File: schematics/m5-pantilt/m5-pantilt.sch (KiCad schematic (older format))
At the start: 23 parts, among them J1 Conn_02x15_Odd_Even, J2 Conn_02x03_Odd_Even, J3 Conn_02x03_Odd_Even, J4 Conn_01x04, J5 BAT, J6 Conn_01x04, J7 5V_POWER, SW1 SW_SPDT, U1 NL27WZ125

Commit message: Update to v0.2.0
Support another Three-State Bus Buffers, TC7WH241FK
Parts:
- added JP10, JP9: Jumper_2_Open, Jumper:SolderJumper-2_P1.3mm_Open_Pad1.0x1.5mm, symbol Jumper:Jumper_2_Open
- U1: value NL27WZ125 -> TC7WH241FK; symbol pantilt:NL27WZ125 -> pantilt:TC7WH241FK
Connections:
- wire segments 117 -> 120
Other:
- moved on the sheet: R1, R2
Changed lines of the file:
@@
 EESchema Schematic File Version 4
-LIBS:m5-pantilt-cache
 EELAYER 30 0
 EELAYER END
@@
 $EndDescr
 $Comp
-L pantilt:NL27WZ125 U1
+L pantilt:TC7WH241FK U1
 U 1 1 60BC20AB
 P 5750 5250
 F 0 "U1" H 5750 5625 50  0000 C CNN
-F 1 "NL27WZ125" H 5750 5534 50  0000 C CNN
+F 1 "TC7WH241FK" H 5750 5534 50  0000 C CNN
 F 2 "m5-pantilt:NL27WZ125USG" H 5500 5650 50  0001 C CNN
 F 3 "" H 5500 5650 50  0001 C CNN
@@
 Wire Wire Line
 	5400 5400 5150 5400
-Wire Wire Line
-	5150 5400 5150 5650
-Wire Wire Line
-	6100 5200 6250 5200
-Wire Wire Line
-	6250 5200 6250 5650
-Wire Wire Line
-	6250 5650 5150 5650
-Connection ~ 5150 5650
-Wire Wire Line
-	5150 5650 5150 5750
 $Comp
 L power:+3.3V #PWR02
@@
 Connection ~ 5150 5400
 Wire Wire Line
-	6100 5300 6450 5300
-Wire Wire Line
-	6100 5400 6450 5400
-Wire Wire Line
-	6450 5400 6450 5300
+	6100 5300 6700 5300
+Wire Wire Line
+	6100 5400 6700 5400
+Wire Wire Line
+	6700 5400 6700 5300
 Wire Wire Line
 	6450 4550 6450 4650
@@
 L Device:R R1
 U 1 1 60BF263A
-P 6450 4900
-F 0 "R1" H 6520 4946 50  0000 L CNN
-F 1 "1k" H 6520 4855 50  0000 L CNN
-F 2 "Resistor_SMD:R_0603_1608Metric_Pad1.05x0.95mm_HandSolder" V 6380 4900 50  0001 C CNN
-F 3 "~" H 6450 4900 50  0001 C CNN
-	1    6450 4900
-	1    0    0    -1
-$EndComp
-Wire Wire Line
-	6450 5050 6450 5150
-Connection ~ 6450 5300
-Wire Wire Line
-	6450 4750 6450 4650
+P 6700 4900
+F 0 "R1" H 6770 4946 50  0000 L CNN
+F 1 "1k" H 6770 4855 50  0000 L CNN
+F 2 "Resistor_SMD:R_0603_1608Metric_Pad1.05x0.95mm_HandSolder" V 6630 4900 50  0001 C CNN
+F 3 "~" H 6700 4900 50  0001 C CNN
+	1    6700 4900
+	1    0    0    -1
+$EndComp
+Wire Wire Line
+	6700 5050 6700 5150
+Connection ~ 6700 5300
 Connection ~ 6450 4650
 $Comp
 L Device:R R2
 U 1 1 60BFA1B3
-P 7050 5150
-F 0 "R2" V 6843 5150 50  0000 C CNN
-F 1 "100" V 6934 5150 50  0000 C CNN
-F 2 "Resistor_SMD:R_0603_1608Metric_Pad1.05x0.95mm_HandSolder" V 6980 5150 50  0001 C CNN
-F 3 "~" H 7050 5150 50  0001 C CNN
-F 4 "https://www.sengoku.co.jp/mod/sgk_cart/detail.php?code=EEHD-57FV" V 7050 5150 50  0001 C CNN "URL"
-	1    7050 5150
+P 7300 5150
+F 0 "R2" V 7093 5150 50  0000 C CNN
+F 1 "100" V 7184 5150 50  0000 C CNN
+F 2 "Resistor_SMD:R_0603_1608Metric_Pad1.05x0.95mm_HandSolder" V 7230 5150 50  0001 C CNN
+F 3 "~" H 7300 5150 50  0001 C CNN
+F 4 "https://www.sengoku.co.jp/mod/sgk_cart/detail.php?code=EEHD-57FV" V 7300 5150 50  0001 C CNN "URL"
+	1    7300 5150
 	0    1    1    0
 $EndComp
 Wire Wire Line
-	6450 5150 6900 5150
-Connection ~ 6450 5150
-Wire Wire Line
-	6450 5150 6450 5300
+	6700 5150 7150 5150
+Connection ~ 6700 5150
+Wire Wire Line
+	6700 5150 6700 5300
 $Comp
 L power:+5V #PWR07
@@
 	7550 4200 7550 5500
 Wire Wire Line
-	7200 5150 9250 5150
+	7450 5150 9250 5150
 Wire Wire Line
 	9250 4400 9250 3900
@@
 Wire Wire Line
 	2300 6400 2300 6500
+Wire Wire Line
+	5150 5400 5150 5600
+$Comp
+L Jumper:Jumper_2_Open JP10
+U 1 1 619167B7
+P 6450 5000
+F 0 "JP10" H 6450 5150 50  0000 C CNN
+F 1 "Jumper_2_Open" H 6400 4900 50  0000 C CNN
+F 2 "Jumper:SolderJumper-2_P1.3mm_Open_Pad1.0x1.5mm" H 6450 5000 50  0001 C CNN
+F 3 "~" H 6450 5000 50  0001 C CNN
+	1    6450 5000
+	0    1    1    0
+$EndComp
+$Comp
+L Jumper:Jumper_2_Open JP9
+U 1 1 61917728
+P 6200 5600
+F 0 "JP9" H 6200 5750 50  0000 C CNN
+F 1 "Jumper_2_Open" H 6150 5500 50  0000 C CNN
+F 2 "Jumper:SolderJumper-2_P1.3mm_Open_Pad1.0x1.5mm" H 6200 5600 50  0001 C CNN
+F 3 "~" H 6200 5600 50  0001 C CNN
+	1    6200 5600
+	1    0    0    -1
+$EndComp
+Wire Wire Line
+	6100 5200 6450 5200
+Wire Wire Line
+	6400 5600 6450 5600
+Wire Wire Line
+	6450 5600 6450 5200
+Connection ~ 6450 5200
+Wire Wire Line
+	5150 5600 6000 5600
+Connection ~ 5150 5600
+Wire Wire Line
+	5150 5600 5150 5750
+Wire Wire Line
+	6450 4800 6450 4650
+Wire Wire Line
+	6450 4650 6700 4650
+Wire Wire Line
+	6700 4650 6700 4750
 $EndSCHEMATC

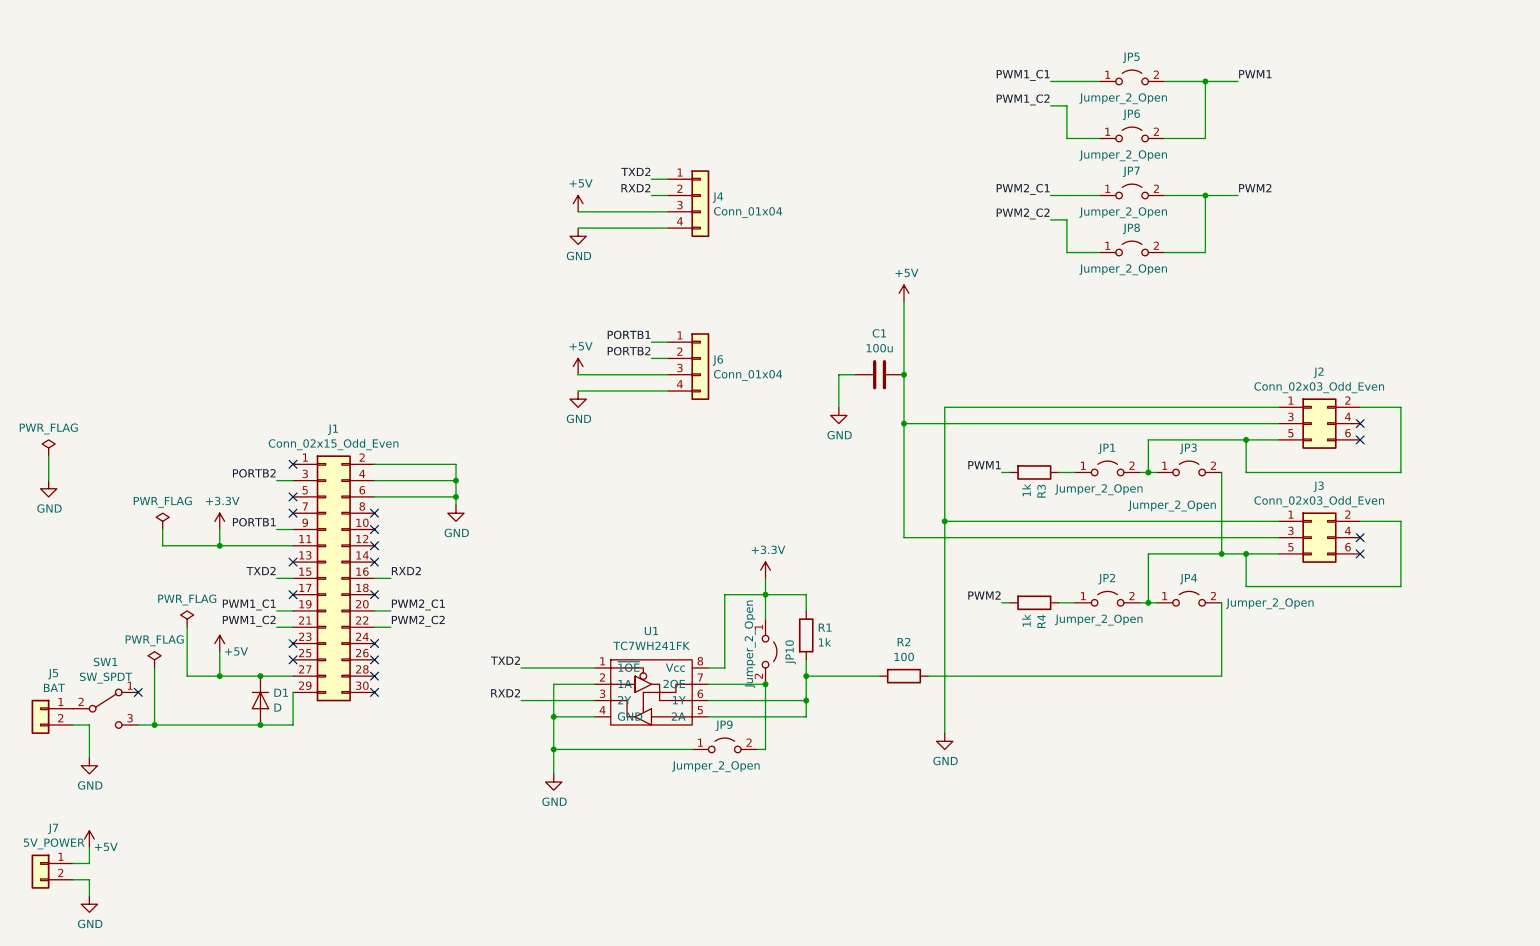
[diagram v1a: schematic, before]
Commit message: Update to v0.2.1
Add description to schematic and PCB
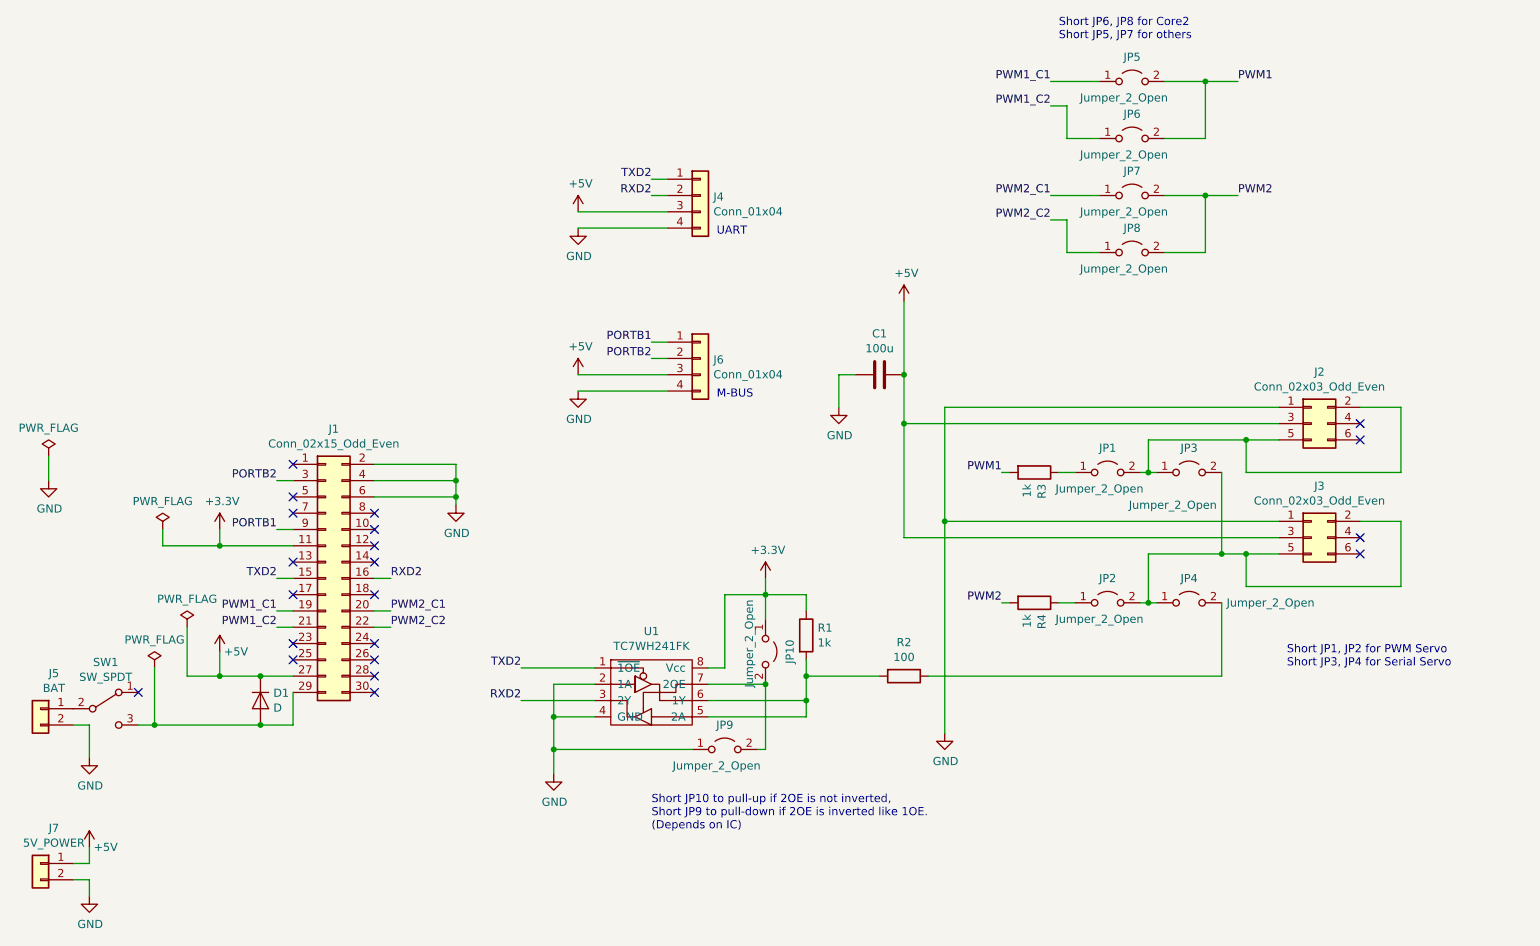
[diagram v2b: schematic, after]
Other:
- note added: "M-BUS"
- note added: "Short JP1, JP2 for PWM Servo\nShort JP3, JP4 for Serial Servo"
- note added: "Short JP10 to pull-up if 2OE is not inverted,\nShort JP9 to pull-down if 2OE is inverted like 1OE.\n(Depends on IC)"
- note added: "Short JP6, JP8 for Core2\nShort JP5, JP7 for others"
- note added: "UART"
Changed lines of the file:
@@
 Wire Wire Line
 	6700 4650 6700 4750
+Text Notes 5750 6100 0    50   ~ 0
+Short JP10 to pull-up if 2OE is not inverted,\nShort JP9 to pull-down if 2OE is inverted like 1OE.\n(Depends on IC)
+Text Notes 8250 1250 0    50   ~ 0
+Short JP6, JP8 for Core2\nShort JP5, JP7 for others
+Text Notes 9650 5100 0    50   ~ 0
+Short JP1, JP2 for PWM Servo\nShort JP3, JP4 for Serial Servo
+Text Notes 6150 3450 0    50   ~ 0
+M-BUS
+Text Notes 6150 2450 0    50   ~ 0
+UART
 $EndSCHEMATC
